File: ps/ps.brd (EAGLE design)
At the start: 99.1 x 54.6 mm, 67 parts, among them IC1 LM675, Q1 NPN-D, Q2 NPN-D, U2 LM317, U3 TLC555CD, U4 LM317, U5 LM317

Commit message: More filtering
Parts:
- added R16: 0.33, rcl:R0805
- C13, C14, C15, C16, C17, C18, C21, C25: value 1u/250V -> 2.2u/250V
- C26: value 0.1uF/250V -> 1uF/100V; device rcl:C1206 -> SparkFun-Capacitors:1210
- L1: value 100u -> 220u; device SparkFun-Passives:B82462G -> my:NR10050T-PTH-ADD
- moved C2 1.27 mm to (17.8, 16.5)
- moved L1 1.27 mm to (6.35, 16.5)
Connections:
- net VCC: now also L1.P$1.1, R16.1
- net VINF: now also L1.P$2.1, R16.2
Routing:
- net VCC: track 20.3 -> 30.7 mm
- net VINF: track 119.0 -> 128.6 mm
- net N$18: track 16.1 -> 15.4 mm
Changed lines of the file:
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@@
 <attribute name="VALUE" x="33.401" y="13.462" size="0.8128" layer="27" ratio="15" rot="R180"/>
 </element>
-<element name="C17" library="rcl" package="C2220K" value="1u/250V" x="46.99" y="35.56" smashed="yes" rot="R270">
+<element name="C17" library="rcl" package="C2220K" value="2.2u/250V" x="46.99" y="35.56" smashed="yes" rot="R270">
 <attribute name="NAME" x="45.46" y="30.89" size="0.8128" layer="25" ratio="15"/>
 <attribute name="VALUE" x="44.19" y="36.03" size="0.8128" layer="27" ratio="15"/>
 </element>
-<element name="C18" library="rcl" package="C2220K" value="1u/250V" x="53.34" y="35.56" smashed="yes" rot="R270">
+<element name="C18" library="rcl" package="C2220K" value="2.2u/250V" x="53.34" y="35.56" smashed="yes" rot="R270">
 <attribute name="NAME" x="51.81" y="30.89" size="0.8128" layer="25" ratio="15"/>
 <attribute name="VALUE" x="50.54" y="34.125" size="0.8128" layer="27" ratio="15"/>
 </element>
-<element name="C21" library="rcl" package="C2220K" value="1u/250V" x="59.69" y="35.56" smashed="yes" rot="R270">
+<element name="C21" library="rcl" package="C2220K" value="2.2u/250V" x="59.69" y="35.56" smashed="yes" rot="R270">
 <attribute name="NAME" x="58.16" y="30.89" size="0.8128" layer="25" ratio="15"/>
 <attribute name="VALUE" x="56.89" y="36.03" size="0.8128" layer="27" ratio="15"/>
@@
 <attribute name="VALUE" x="78.74" y="34.29" size="0.8128" layer="27" ratio="15" rot="R90"/>
 </element>
-<element name="C25" library="rcl" package="C2220K" value="1u/250V" x="66.04" y="35.56" smashed="yes" rot="R270">
+<element name="C25" library="rcl" package="C2220K" value="2.2u/250V" x="66.04" y="35.56" smashed="yes" rot="R270">
 <attribute name="NAME" x="64.51" y="30.89" size="0.8128" layer="25" ratio="15"/>
 <attribute name="VALUE" x="63.24" y="34.125" size="0.8128" layer="27" ratio="15"/>
 </element>
-<element name="C26" library="rcl" package="C1206" value="0.1uF/250V" x="72.39" y="21.59" smashed="yes" rot="R90">
-<attribute name="NAME" x="71.12" y="20.32" size="0.8128" layer="25" ratio="15" rot="R90"/>
-<attribute name="VALUE" x="74.295" y="20.32" size="0.8128" layer="27" ratio="15" rot="R90"/>
+<element name="C26" library="SparkFun-Capacitors" package="1210" value="1uF/100V" x="72.39" y="21.59" smashed="yes" rot="R90">
+<attribute name="NAME" x="73.66" y="25.4" size="0.8128" layer="25" ratio="15" rot="R180"/>
 </element>
 <element name="C27" library="rcl" package="C2220K" value="2.2uF/250V" x="53.34" y="22.86" smashed="yes" rot="R90">
@@
 <attribute name="VALUE" x="47.244" y="12.827" size="0.8128" layer="27" font="vector" ratio="15"/>
 </element>
-<element name="C13" library="rcl" package="C2220K" value="1u/250V" x="21.59" y="35.56" smashed="yes" rot="R270">
+<element name="C13" library="rcl" package="C2220K" value="2.2u/250V" x="21.59" y="35.56" smashed="yes" rot="R270">
 <attribute name="NAME" x="20.06" y="30.89" size="0.8128" layer="25" ratio="15"/>
 <attribute name="VALUE" x="18.79" y="36.03" size="0.8128" layer="27" ratio="15"/>
 </element>
-<element name="C14" library="rcl" package="C2220K" value="1u/250V" x="27.94" y="35.56" smashed="yes" rot="R270">
+<element name="C14" library="rcl" package="C2220K" value="2.2u/250V" x="27.94" y="35.56" smashed="yes" rot="R270">
 <attribute name="NAME" x="26.41" y="30.89" size="0.8128" layer="25" ratio="15"/>
 <attribute name="VALUE" x="23.87" y="34.125" size="0.8128" layer="27" ratio="15"/>
 </element>
-<element name="C15" library="rcl" package="C2220K" value="1u/250V" x="34.29" y="35.56" smashed="yes" rot="R270">
+<element name="C15" library="rcl" package="C2220K" value="2.2u/250V" x="34.29" y="35.56" smashed="yes" rot="R270">
 <attribute name="NAME" x="32.76" y="30.89" size="0.8128" layer="25" ratio="15"/>
 <attribute name="VALUE" x="31.49" y="36.03" size="0.8128" layer="27" ratio="15"/>
 </element>
-<element name="C16" library="rcl" package="C2220K" value="1u/250V" x="40.64" y="35.56" smashed="yes" rot="R270">
+<element name="C16" library="rcl" package="C2220K" value="2.2u/250V" x="40.64" y="35.56" smashed="yes" rot="R270">
 <attribute name="NAME" x="39.11" y="30.89" size="0.8128" layer="25" ratio="15"/>
 <attribute name="VALUE" x="37.205" y="34.125" size="0.8128" layer="27" ratio="15"/>
@@
 <attribute name="VALUE" x="19.812" y="25.654" size="0.8128" layer="27" ratio="15" rot="R90"/>
 </element>
-<element name="L1" library="SparkFun-Passives" package="B82462G" value="100u" x="6.35" y="17.78" rot="R180"/>
-<element name="C2" library="SparkFun-Capacitors" package="CPOL-RADIAL-1000UF-25V" value="470uF" x="16.51" y="16.51" smashed="yes" rot="R180">
-<attribute name="VALUE" x="18.415" y="20.828" size="0.8128" layer="27" ratio="15" rot="R180"/>
-<attribute name="NAME" x="17.272" y="13.589" size="0.8128" layer="25" ratio="15" rot="R180"/>
+<element name="L1" library="my" package="NR10050T-PTH-ADD" value="220u" x="6.35" y="16.51" rot="R180"/>
+<element name="C2" library="SparkFun-Capacitors" package="CPOL-RADIAL-1000UF-25V" value="470uF" x="17.78" y="16.51" smashed="yes" rot="R180">
+<attribute name="VALUE" x="19.685" y="20.828" size="0.8128" layer="27" ratio="15" rot="R180"/>
+<attribute name="NAME" x="18.542" y="13.589" size="0.8128" layer="25" ratio="15" rot="R180"/>
 </element>
 <element name="C20" library="SparkFun-Capacitors" package="CPOL-RADIAL-1000UF-25V" value="470uF" x="88.9" y="8.89" smashed="yes" rot="R180">
@@
 </element>
 <element name="R15" library="SparkFun-Resistors" package="AXIAL-0.5" value="6.8/0.5W" x="10.16" y="42.545" rot="R180"/>
+<element name="R16" library="rcl" package="R0805" value="0.33" x="12.065" y="22.225" smashed="yes">
+<attribute name="NAME" x="12.065" y="23.495" size="0.8128" layer="25" ratio="15"/>
+<attribute name="VALUE" x="10.795" y="20.32" size="0.8128" layer="27" ratio="15"/>
+</element>
 </elements>
 <signals>
@@
 <via x="25.4" y="8.89" extent="1-16" drill="0.6"/>
 <via x="21.59" y="11.43" extent="1-16" drill="0.6"/>
-<via x="11.43" y="19.05" extent="1-16" drill="0.6"/>
+<via x="17.78" y="20.32" extent="1-16" drill="0.6"/>
 <via x="17.78" y="13.97" extent="1-16" drill="0.6"/>
 <via x="10.16" y="27.94" extent="1-16" drill="0.6"/>
@@
 <contactref element="R12" pad="P$1"/>
 <contactref element="C26" pad="1"/>
-<wire x1="72" y1="20.58" x2="72.39" y2="20.19" width="0.6096" layer="1" curve="-90"/>
-<wire x1="72.39" y1="20.19" x2="72.39" y2="16.51" width="0.6096" layer="1"/>
 <wire x1="72.39" y1="16.51" x2="76.2" y2="16.51" width="0.6096" layer="1"/>
 <wire x1="76.2" y1="16.51" x2="80.01" y2="16.51" width="0.6096" layer="1"/>
 <wire x1="68.3" y1="20.58" x2="68.69" y2="20.19" width="0.6096" layer="1" curve="90"/>
-<wire x1="68.69" y1="20.19" x2="72.39" y2="20.19" width="0.6096" layer="1"/>
+<wire x1="68.69" y1="20.19" x2="68.89" y2="19.99" width="0.6096" layer="1" curve="90"/>
+<wire x1="68.89" y1="19.99" x2="72.39" y2="19.99" width="0.6096" layer="1"/>
+<wire x1="72.39" y1="19.99" x2="72.39" y2="16.51" width="0.6096" layer="1"/>
 </signal>
 <signal name="HT" class="1">
@@
 <via x="29.21" y="24.13" extent="1-16" drill="0.6"/>
 <contactref element="U4" pad="3"/>
-<wire x1="6.35" y1="20.53" x2="12.7" y2="26.88" width="1.27" layer="1" curve="90"/>
 <wire x1="12.7" y1="26.88" x2="12.7" y2="31.75" width="1.27" layer="1"/>
 <wire x1="22.301" y1="24.13" x2="17.78" y2="24.13" width="1.27" layer="1"/>
@@
 <wire x1="24.765" y1="16.93" x2="25.361" y2="16.93" width="0.6096" layer="1"/>
 <wire x1="25.361" y1="16.93" x2="26.416" y2="15.875" width="0.6096" layer="1" curve="-90"/>
+<contactref element="R16" pad="2"/>
+<contactref element="L1" pad="P$2.1"/>
+<wire x1="12.7" y1="26.86" x2="12.7" y2="26.88" width="1.27" layer="1"/>
+<wire x1="6.35" y1="20.51" x2="6.35" y2="25.4" width="1.27" layer="1"/>
+<wire x1="6.35" y1="25.4" x2="12.7" y2="31.75" width="1.27" layer="1" curve="-90"/>
+<wire x1="13.015" y1="22.225" x2="13.545" y2="22.225" width="1.27" layer="1"/>
+<wire x1="13.545" y1="22.225" x2="15.45" y2="24.13" width="1.27" layer="1" curve="90"/>
+<wire x1="6.35" y1="19.01" x2="6.35" y2="20.51" width="1.27" layer="1"/>
 </signal>
 <signal name="VREG" class="1">
@@
 <contactref element="L1" pad="P$1"/>
 <contactref element="X1" pad="1"/>
-<wire x1="13.97" y1="4.445" x2="13.97" y2="16.51" width="1.27" layer="1"/>
-<wire x1="13.97" y1="16.51" x2="12.49" y2="15.03" width="1.27" layer="1" curve="-90"/>
-<wire x1="12.49" y1="15.03" x2="6.35" y2="15.03" width="1.27" layer="1"/>
+<contactref element="R16" pad="1"/>
+<contactref element="L1" pad="P$1.1"/>
+<wire x1="6.35" y1="12.51" x2="11.24" y2="12.51" width="1.27" layer="1"/>
+<wire x1="11.24" y1="12.51" x2="15.24" y2="16.51" width="1.27" layer="1" curve="90"/>
+<wire x1="11.115" y1="22.225" x2="11.115" y2="20.635" width="1.27" layer="1"/>
+<wire x1="11.115" y1="20.635" x2="15.24" y2="16.51" width="1.27" layer="1" curve="90"/>
+<wire x1="13.97" y1="4.445" x2="6.35" y2="12.065" width="1.27" layer="1" curve="-90"/>
+<wire x1="6.35" y1="12.065" x2="6.35" y2="12.51" width="1.27" layer="1"/>
+<wire x1="6.35" y1="14.01" x2="6.35" y2="12.51" width="1.27" layer="1"/>
 </signal>
 <signal name="H+">

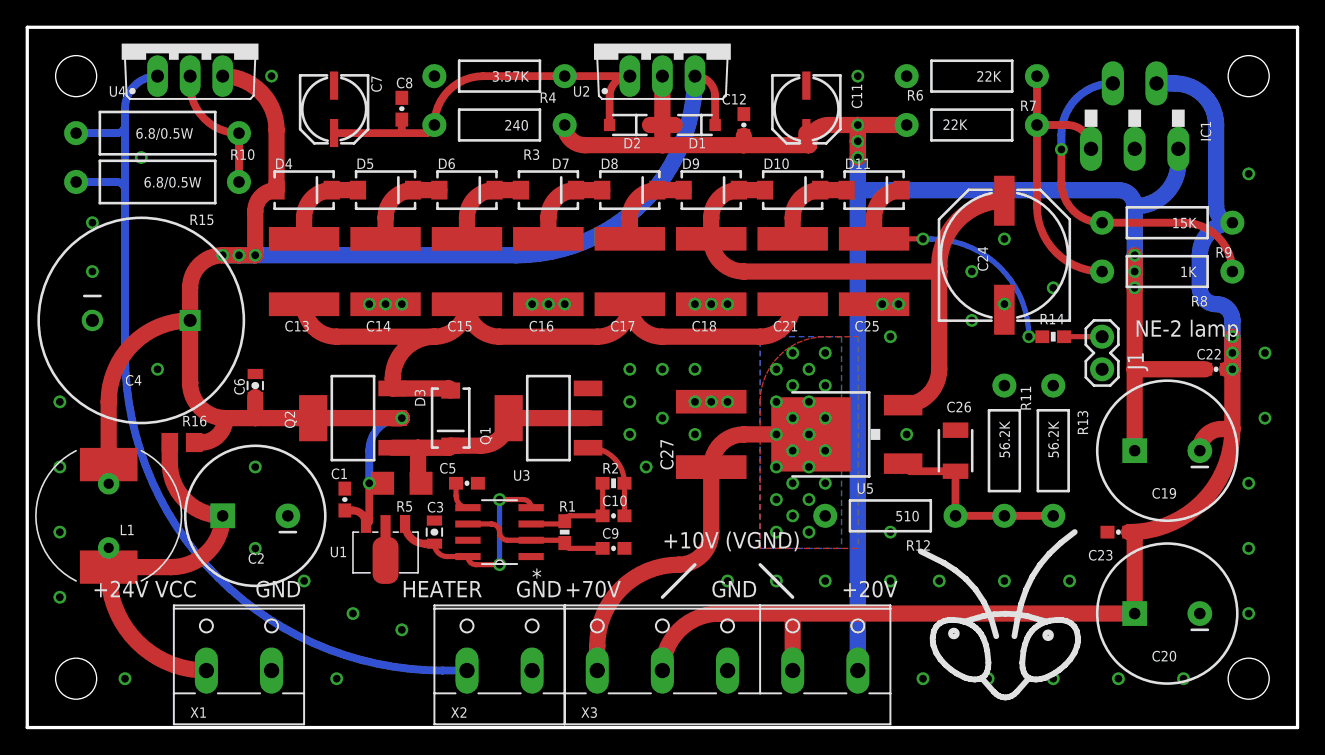
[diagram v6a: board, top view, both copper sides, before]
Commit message: HT filter added
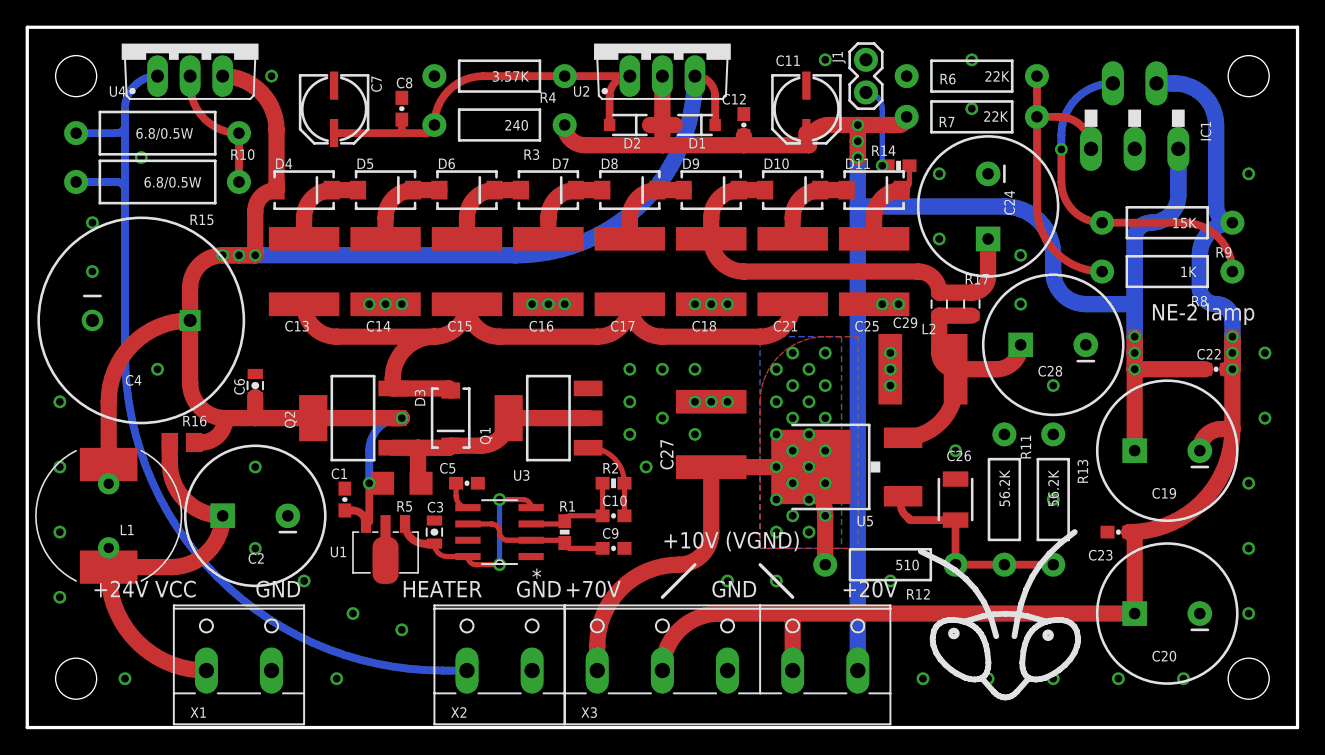
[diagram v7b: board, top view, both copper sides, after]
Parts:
- added C28: 100uF/160V, SparkFun-Capacitors:CPOL-RADIAL-1000UF-25V
- added C29: 1uF/250V, rcl:C2220K
- added L2: 10u, SparkFun-Passives:0805
- added R17: 0.33, SparkFun-Resistors:0805
- C24: value 10uF/250V -> 10uF/160V; device SparkFun-Capacitors:PANASONIC_G -> SparkFun-Capacitors:CPOL-RADIAL-1000UF-25V
- moved J1 30.4 mm to (65.4, 52.1), turned to 270 degrees
- moved R14 18.0 mm to (67.9, 43.8), turned to 0 degrees
- moved C24 4.02 mm to (74.9, 40.6), turned to 270 degrees
- moved R12 3.81 mm to (67.3, 12.7)
- moved C26 3.81 mm to (72.4, 17.8)
- moved R11 3.81 mm to (76.2, 17.8)
- moved R13 3.81 mm to (80.0, 17.8)
- moved U5 2.54 mm to (63.5, 20.3)
- moved R6 0.63 mm to (73.7, 47.6)
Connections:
- new net N$7: C28.+, C29.1, L2.2, R17.2, U5.3
- net GND: now also C28.-, C29.2
- net N$15: now also L2.1, R17.1; no longer U5.3
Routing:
- net N$7: track 0.00 -> 20.1 mm
- net HV: track 21.0 -> 6.85 mm, vias 2 -> 0
- net N$15: track 44.8 -> 33.5 mm
- net HT: track 28.4 -> 33.8 mm, vias 23 -> 24
- net N$5: track 2.96 -> 6.66 mm, vias 0 -> 1
- net VREG: track 137.2 -> 140.9 mm
- net N$18: track 15.4 -> 16.6 mm
